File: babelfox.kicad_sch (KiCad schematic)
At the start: 41 parts, among them J1 DCIN, J2 Battery, J3 GPIO, J4 Qwiic, J5 RJ45_Bel_SI-60062-F, J6 LoRA 900 SMA, J7 LoRA 2.4G ANT, J8 Cellular Ant, J9 LoRA 900 u.FL, Q1 FZ788B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

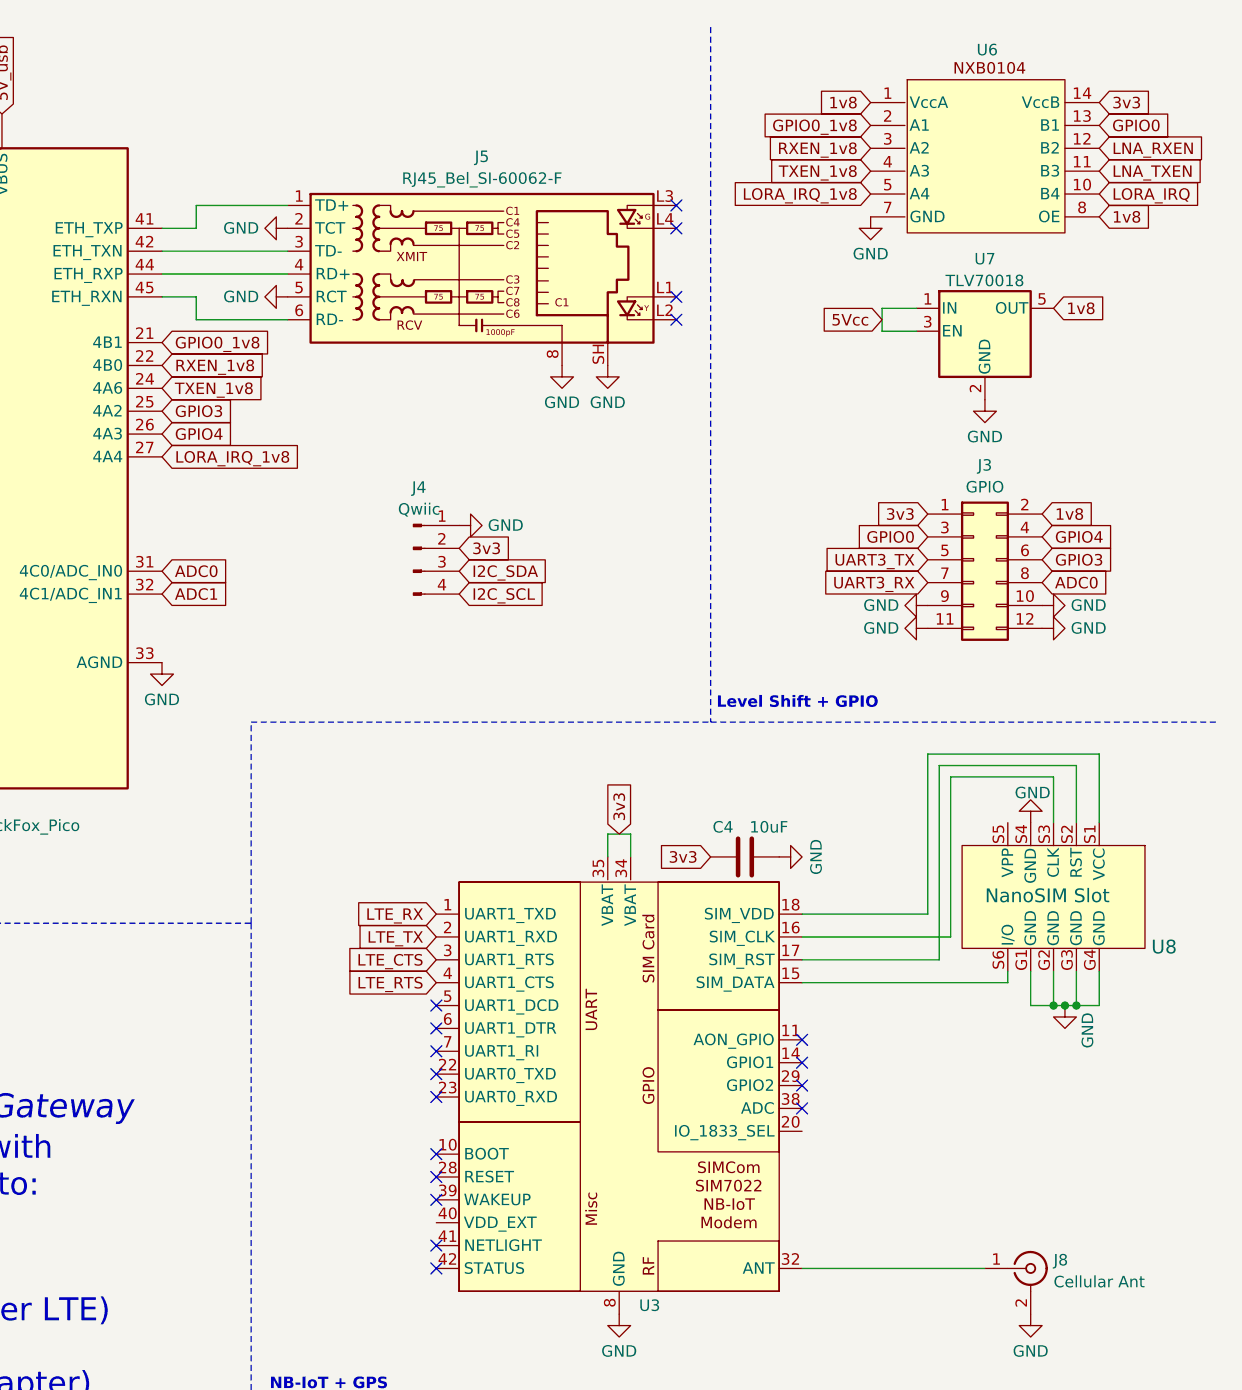
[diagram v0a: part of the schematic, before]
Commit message: Jan 5 progress, update license to OHL-S
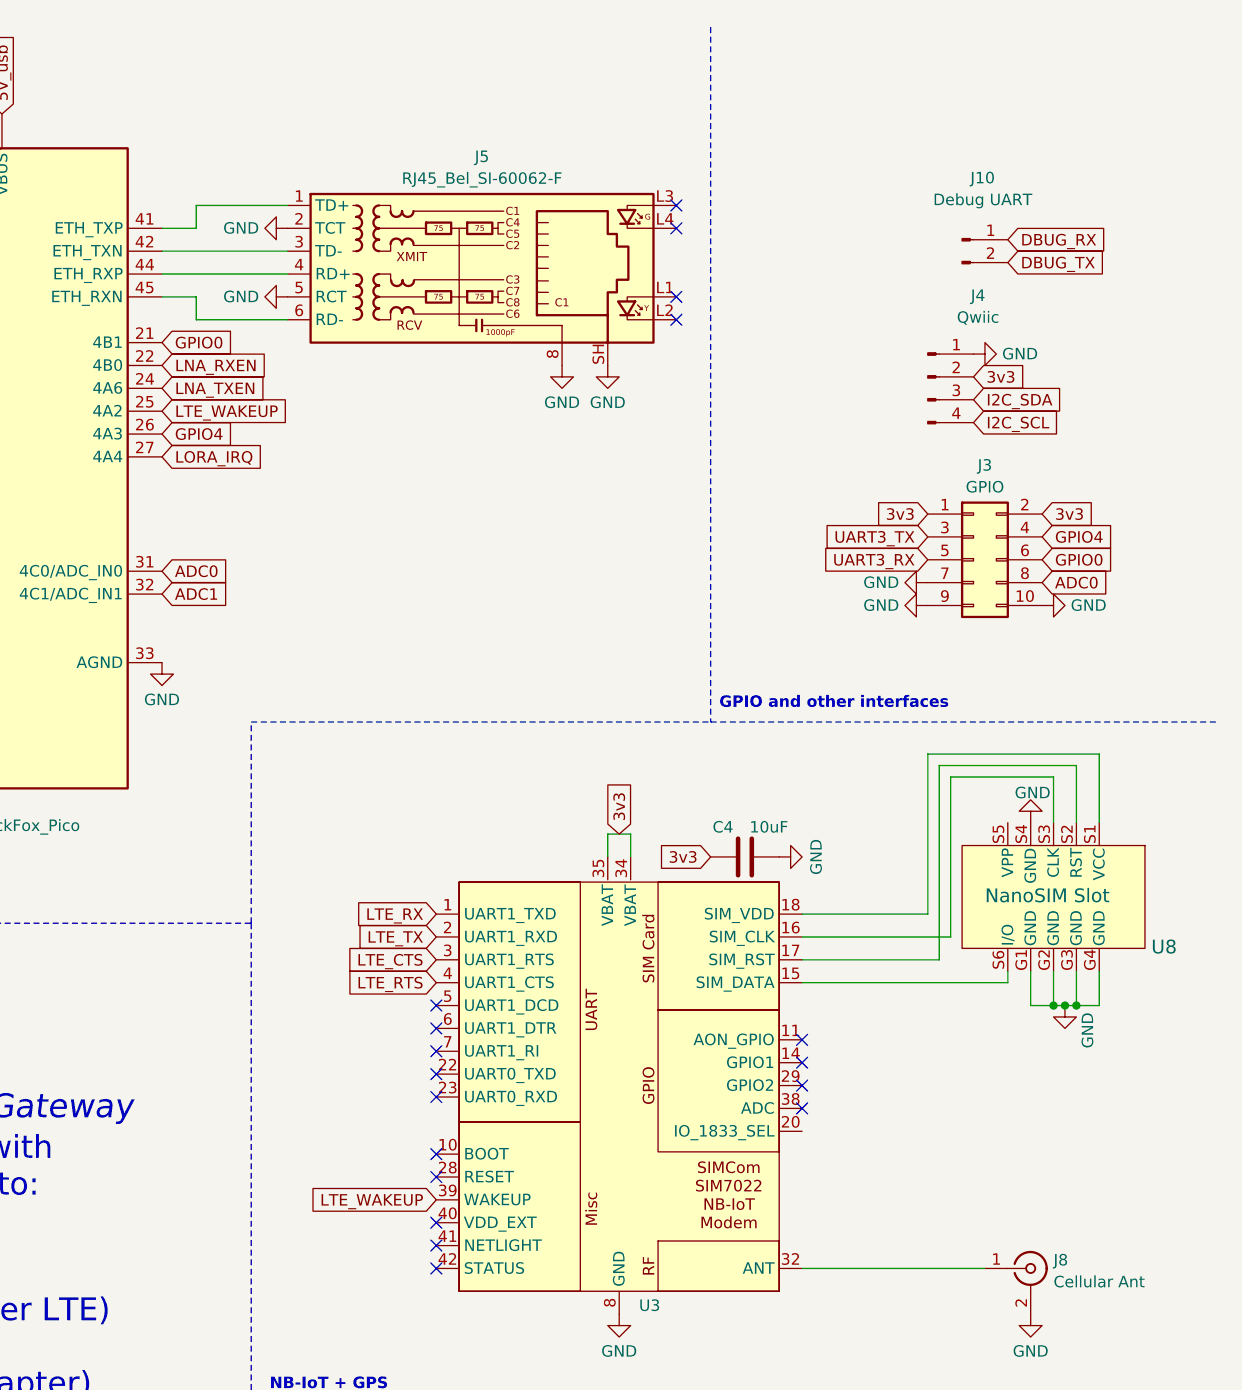
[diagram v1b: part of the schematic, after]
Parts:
- removed J3: GPIO, Connector_PinHeader_2.54mm:PinHeader_2x06_P2.54mm_Vertical, symbol Connector_Generic:Conn_02x06_Odd_Even
- removed U6: ~, Package_SO:TSSOP-14_4.4x5mm_P0.65mm, symbol NXB0104:NXB0104
- removed U7: TLV70018, Package_TO_SOT_SMD:SOT-23-5, symbol Regulator_Linear:TLV70018_SOT23-5
- added J10: Debug UART, Connector_PinSocket_2.54mm:PinSocket_1x02_P2.54mm_Vertical, symbol Connector:Conn_01x02_Pin
- added J3: GPIO, Connector_PinHeader_2.54mm:PinHeader_2x05_P2.54mm_Vertical, symbol Connector_Generic:Conn_02x05_Odd_Even
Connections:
- net GPIO0_1v8 is gone; now on net GPIO0: U2.21 (4B1)
- net GPIO3 is gone; now on net LTE_WAKEUP: U2.25 (4A2)
- net LORA_IRQ_1v8 is gone; now on net LORA_IRQ: U2.27 (4A4)
- net RXEN_1v8 is gone; now on net LNA_RXEN: U2.22 (4B0)
- net TXEN_1v8 is gone; now on net LNA_TXEN: U2.24 (4A6)
- net 3v3: now also J3.1 (Pin_1), J3.2 (Pin_2)
- net ADC0: now also J3.8 (Pin_8)
- net DBUG_RX: now also J10.1 (Pin_1)
- net DBUG_TX: now also J10.2 (Pin_2)
- net GND: now also J3.10 (Pin_10), J3.7 (Pin_7), J3.9 (Pin_9)
- net GPIO0: now also J3.6 (Pin_6)
- net GPIO4: now also J3.4 (Pin_4)
- net UART3_RX: now also J3.5 (Pin_5)
- net UART3_TX: now also J3.3 (Pin_3)
- net LTE_WAKEUP: now reaches U3.39 (WAKEUP)
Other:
- note added: "GPIO and other interfaces"
- note removed: "Level Shift + GPIO"
- moved on the sheet: J4

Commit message: LCSC IDs; OSHW silkscreen; new imgs
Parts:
- C1: LCSC (none) -> C141660
- C2, C3, C4, C5, C6, C8: LCSC (none) -> C15850
- C7: LCSC (none) -> C17604
- D1, D2: LCSC (none) -> C511853
- D3: LCSC (none) -> C5156920
- J9: LCSC (none) -> C88373
- Q1: LCSC (none) -> C141330
- R1: LCSC (none) -> C2999620
- R2: LCSC (none) -> C4407
- R3: LCSC (none) -> C44051
- R4, R5, R6: LCSC (none) -> C17513
- R8: LCSC (none) -> C25611
- R9: LCSC (none) -> C17470
- U1: LCSC (none) -> C5219190
- U8: LCSC (none) -> C585349
- U9: LCSC (none) -> C2866550
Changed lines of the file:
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@@
 			)
 		)
+		(property "LCSC" "C4407"
+			(at 63.5 59.69 0)
+			(effects
+				(font
+					(size 1.27 1.27)
+				)
+				(hide yes)
+			)
+		)
 		(pin "2"
 		)
@@
 			)
 		)
+		(property "LCSC" "C585349"
+			(at 271.78 95.25 90)
+			(effects
+				(font
+					(size 1.27 1.27)
+				)
+				(hide yes)
+			)
+		)
 		(pin "G4"
 		)
@@
 			)
 		)
+		(property "LCSC" "C511853"
+			(at 64.77 100.33 0)
+			(effects
+				(font
+					(size 1.27 1.27)
+				)
+				(hide yes)
+			)
+		)
 		(pin "2"
 		)
@@
 			)
 		)
+		(property "LCSC" "C15850"
+			(at 20.32 24.13 0)
+			(effects
+				(font
+					(size 1.27 1.27)
+				)
+				(hide yes)
+			)
+		)
 		(pin "1"
 		)
@@
 			)
 		)
+		(property "LCSC" "C17513"
+			(at 15.24 90.17 0)
+			(effects
+				(font
+					(size 1.27 1.27)
+				)
+				(hide yes)
+			)
+		)
 		(pin "2"
 		)
@@
 			)
 		)
+		(property "LCSC" "C2999620"
+			(at 63.5 52.07 0)
+			(effects
+				(font
+					(size 1.27 1.27)
+				)
+				(hide yes)
+			)
+		)
 		(pin "2"
 		)
@@
 			)
 		)
+		(property "LCSC" "C17513"
+			(at 15.24 97.79 0)
+			(effects
+				(font
+					(size 1.27 1.27)
+				)
+				(hide yes)
+			)
+		)
 		(pin "2"
 		)
@@
 			)
 		)
+		(property "LCSC" "C2866550"
+			(at 33.02 95.25 0)
+			(effects
+				(font
+					(size 1.27 1.27)
+				)
+				(hide yes)
+			)
+		)
 		(pin "1"
 		)
@@
 			)
 		)
+		(property "LCSC" "C88373"
+			(at 82.55 133.35 0)
+			(effects
+				(font
+					(size 1.27 1.27)
+				)
+				(hide yes)
+			)
+		)
 		(pin "2"
 		)
@@
 			)
 		)
+		(property "LCSC" "C5219190"
+			(at 44.45 54.61 0)
+			(effects
+				(font
+					(size 1.27 1.27)
+				)
+				(hide yes)
+			)
+		)
 		(pin "2"
 		)
@@
 			)
 		)
+		(property "LCSC" "C15850"
+			(at 86.36 158.75 0)
+			(effects
+				(font
+					(size 1.27 1.27)
+				)
+				(hide yes)
+			)
+		)
 		(pin "1"
 		)
@@
 			)
 		)
+		(property "LCSC" "C17470"
+			(at 87.63 48.26 0)
+			(effects
+				(font
+					(size 1.27 1.27)
+				)
+				(hide yes)
+			)
+		)
 		(pin "2"
 		)
@@
 			)
 		)
+		(property "LCSC" "C25611"
+			(at 87.63 55.88 0)
+			(effects
+				(font
+					(size 1.27 1.27)
+				)
+				(hide yes)
+			)
+		)
 		(pin "2"
 		)
@@
 			)
 		)
+		(property "LCSC" "C15850"
+			(at 232.41 104.14 90)
+			(effects
+				(font
+					(size 1.27 1.27)
+				)
+				(hide yes)
+			)
+		)
 		(pin "1"
 		)
@@
 			)
 		)
+		(property "LCSC" "C44051"
+			(at 39.37 78.74 90)
+			(effects
+				(font
+					(size 1.27 1.27)
+				)
+				(hide yes)
+			)
+		)
 		(pin "1"
 		)
@@
 			)
 		)
+		(property "LCSC" "C17604"
+			(at 81.28 86.36 0)
+			(effects
+				(font
+					(size 1.27 1.27)
+				)
+				(hide yes)
+			)
+		)
 		(pin "2"
 		)
@@
 			)
 		)
+		(property "LCSC" "C5156920"
+			(at 41.91 97.79 90)
+			(effects
+				(font
+					(size 1.27 1.27)
+				)
+				(hide yes)
+			)
+		)
 		(pin "1"
 		)
@@
 			)
 		)
+		(property "LCSC" "C141330"
+			(at 60.96 81.28 90)
+			(effects
+				(font
+					(size 1.27 1.27)
+				)
+				(hide yes)
+			)
+		)
 		(pin "1"
 		)
@@
 			)
 		)
+		(property "LCSC" "C17513"
+			(at 52.07 88.9 90)
+			(effects
+				(font
+					(size 1.27 1.27)
+				)
+				(hide yes)
+			)
+		)
 		(pin "2"
 		)
@@
 			)
 		)
+		(property "LCSC" "C15850"
+			(at 17.78 133.35 0)
+			(effects
+				(font
+					(size 1.27 1.27)
+				)
+				(hide yes)
+			)
+		)
 		(pin "1"
 		)
@@
 			)
 		)
+		(property "LCSC" "C511853"
+			(at 64.77 105.41 0)
+			(effects
+				(font
+					(size 1.27 1.27)
+				)
+				(hide yes)
+			)
+		)
 		(pin "2"
 		)
@@
 			)
 		)
+		(property "LCSC" "C15850"
+			(at 57.15 24.13 0)
+			(effects
+				(font
+					(size 1.27 1.27)
+				)
+				(hide yes)
+			)
+		)
 		(pin "1"
 		)
@@
 			)
 		)
+		(property "LCSC" "C15850"
+			(at 19.05 54.61 0)
+			(effects
+				(font
+					(size 1.27 1.27)
+				)
+				(hide yes)
+			)
+		)
 		(pin "2"
 		)
@@
 			(at 76.2 52.07 0)
 			(effects
+				(font
+					(size 1.27 1.27)
+				)
+				(hide yes)
+			)
+		)
+		(property "LCSC" "C141660"
+			(at 76.2 52.07 0)
+			(effects

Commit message: LCSC inductor... but i'm not doing LCSC anymore
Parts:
- L1: LCSC (none) -> C76827
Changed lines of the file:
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@@
+			)
+		)
+		(property "LCSC" "C76827"
+			(at 44.45 36.83 90)
+			(effects
+				(font
+					(size 1.27 1.27)
+				)
+				(hide yes)
 			)
 		)

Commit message: board as sent to JLC 1/11
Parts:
- C1: Notes (none) -> 6V, DNP if no battery circuit
- C2, C3, C4, C5, C6, C8: Notes (none) -> 25V, qty 5 if no battery circuit
- C7, J2, Q1, R1, R2, R3, R4, R5, R6, R7, R8, R9: Notes (none) -> DNP if no battery circuit
- D1, D2: Notes (none) -> 30V
- J6, J7: Notes (none) -> SMA with pre-wired u.FL/IPEX pigtail
- L1: Notes (none) -> Isat > 3A, DNP if no battery circuit
- U1: value ~ -> TPS631000; Notes (none) -> DNP if no battery circuit
- U10: Notes (none) -> >1.5A output recommended
- U3: value ~ -> SIM7022
- U4: value ~ -> E80-900M2213S
- U5: value ~ -> E21-900G30S
- U9: value ~ -> BQ2057CSNTR; Notes (none) -> DNP if no battery circuit
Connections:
- net 3v3: no longer J3.2 (Pin_2)
- net 5Vcc: now also J3.2 (Pin_2)
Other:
- moved on the sheet: C3, C7, J10

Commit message: push BOM
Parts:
- C2, C3, C4, C5, C6, C8: Notes 25V, qty 5 if no battery circuit -> 25V, qty 3 if no battery circuit
- D1, D2: Notes 30V -> 30V, >2A, low Vdrop
- D3: Notes (none) -> DNP if no battery circuit
- Q1, R1, R3, R8, R9: Notes DNP if no battery circuit -> 1% or better, DNP if no battery circuit
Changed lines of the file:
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@@
 			)
 		)
-		(property "Notes" "30V"
+		(property "Notes" "30V, >2A, low Vdrop"
 			(at 64.77 100.33 0)
 			(effects
@@
 			)
 		)
-		(property "Notes" "25V, qty 5 if no battery circuit"
+		(property "Notes" "25V, qty 3 if no battery circuit"
 			(at 20.32 24.13 0)
 			(effects
@@
 			)
 		)
-		(property "Notes" "DNP if no battery circuit"
+		(property "Notes" "1% or better, DNP if no battery circuit"
 			(at 63.5 52.07 0)
 			(effects
@@
 			)
 		)
-		(property "Notes" "25V, qty 5 if no battery circuit"
+		(property "Notes" "25V, qty 3 if no battery circuit"
 			(at 82.55 158.75 0)
 			(effects
@@
 			)
 		)
-		(property "Notes" "DNP if no battery circuit"
+		(property "Notes" "1% or better, DNP if no battery circuit"
 			(at 87.63 48.26 0)
 			(effects
@@
 			)
 		)
-		(property "Notes" "DNP if no battery circuit"
+		(property "Notes" "1% or better, DNP if no battery circuit"
 			(at 87.63 55.88 0)
 			(effects
@@
 			)
 		)
-		(property "Notes" "25V, qty 5 if no battery circuit"
+		(property "Notes" "25V, qty 3 if no battery circuit"
 			(at 232.41 104.14 0)
 			(effects
@@
 			)
 		)
-		(property "Notes" "DNP if no battery circuit"
+		(property "Notes" "1% or better, DNP if no battery circuit"
 			(at 39.37 78.74 0)
 			(effects
@@
 			)
 		)
-		(property "Notes" ""
+		(property "Notes" "DNP if no battery circuit"
 			(at 41.91 97.79 0)
 			(effects
@@
 			)
 		)
-		(property "Notes" "DNP if no battery circuit"
+		(property "Notes" "1% or better, DNP if no battery circuit"
 			(at 60.96 81.28 0)
 			(effects
@@
 			)
 		)
-		(property "Notes" "25V, qty 5 if no battery circuit"
+		(property "Notes" "25V, qty 3 if no battery circuit"
 			(at 17.78 133.35 0)
 			(effects
@@
 			)
 		)
-		(property "Notes" "30V"
+		(property "Notes" "30V, >2A, low Vdrop"
 			(at 64.77 105.41 0)
 			(effects
@@
 			)
 		)
-		(property "Notes" "25V, qty 5 if no battery circuit"
+		(property "Notes" "25V, qty 3 if no battery circuit"
 			(at 57.15 24.13 0)
 			(effects
@@
 			)
 		)
-		(property "Notes" "25V, qty 5 if no battery circuit"
+		(property "Notes" "25V, qty 3 if no battery circuit"
 			(at 19.05 54.61 0)
 			(effects
